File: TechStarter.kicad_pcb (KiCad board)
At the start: 2 copper layers, 57 parts, among them J10 Conn_01x03_Socket, J11 Conn_01x03_Socket, J3 Conn_01x02_Socket, J5 Conn_01x03_Socket, J7 Conn_01x03_Socket, J8 Conn_01x03_Socket, J9 Conn_01x03_Socket, Q3 IRLZ44N, U1 STM32F446RETx, U10 PC817, U2 TMC2209-LA, U3 TMC2209-LA, U4 LM2596S-3.3, U5 MX25L3233FM1, U6 TMC2209-LA, U7 AMS1117-3.3, U8 TMC2209-LA, U9 PC817

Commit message: .
.
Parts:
- removed BT1: Battery_Cell, Battery:BatteryHolder_ComfortableElectronic_CH273-2450_1x2450
- added C17: 680uF/35V, Capacitor_SMD:C_Elec_10x10.2, F.Cu at (150.1, 43.5)
- added C18: 220nF/6,3V, Capacitor_SMD:C_0603_1608Metric, F.Cu at (69.4, 102.5)
- added C19: 220nF/6,3V, Capacitor_SMD:C_0603_1608Metric, F.Cu at (69.4, 105.0)
- added C20: 220nF/6,3V, Capacitor_SMD:C_0603_1608Metric, F.Cu at (131.5, 126.5)
- added C21: 4,7uF, Capacitor_SMD:C_Elec_10x10.2, F.Cu at (200.5, 163.5)
- added C22: 220nF/6,3V, Capacitor_SMD:C_0603_1608Metric, F.Cu at (143.2, 75.5)
- added C23: 220nF/6,3V, Capacitor_SMD:C_0603_1608Metric, F.Cu at (143.2, 78.0)
- added J1: Conn_01x04_Socket, Connector_Phoenix_MC:PhoenixContact_MC_1,5_4-GF-3.81_1x04_P3.81mm_Horizontal_ThreadedFlange_MountHole, F.Cu at (261.0, 70.4)
- added J12: Conn_01x04_Pin, Connector_PinSocket_2.54mm:PinSocket_1x04_P2.54mm_Vertical_SMD_Pin1Left, F.Cu at (87.5, 122.0)
- added J13: Conn_01x02_Socket, Connector_Phoenix_MC:PhoenixContact_MC_1,5_2-GF-3.5_1x02_P3.50mm_Horizontal_ThreadedFlange_MountHole, F.Cu at (175.7, 29.4)
- added J14: Conn_01x04_Socket, Connector_JST:JST_XH_B4B-XH-A_1x04_P2.50mm_Vertical, F.Cu at (237.0, 127.8)
- added J15: Conn_01x04_Socket, Connector_JST:JST_XH_S4B-XH-A_1x04_P2.50mm_Horizontal, F.Cu at (230.2, 134.8)
- added J16: Conn_01x02_Socket, Connector_Phoenix_MC:PhoenixContact_MC_1,5_2-G-3.81_1x02_P3.81mm_Horizontal, F.Cu at (190.3, 29.4)
- added J17: Conn_01x02_Socket, Connector_JST:JST_XH_B2B-XH-A_1x02_P2.50mm_Vertical, F.Cu at (172.5, 124.2)
- added J18: Conn_01x04_Socket, Connector_JST:JST_XH_S4B-XH-A_1x04_P2.50mm_Horizontal, F.Cu at (243.8, 134.8)
- added J2: Conn_01x04_Socket, Connector_Phoenix_MC:PhoenixContact_MC_1,5_4-GF-3.81_1x04_P3.81mm_Horizontal_ThreadedFlange_MountHole, F.Cu at (261.1, 43.7)
- added J4: Conn_01x04_Socket, Connector_Phoenix_MC:PhoenixContact_MC_1,5_4-GF-3.81_1x04_P3.81mm_Horizontal_ThreadedFlange_MountHole, F.Cu at (261.0, 97.4)
- added J6: Conn_01x04_Socket, Connector_Phoenix_MC:PhoenixContact_MC_1,5_4-GF-3.81_1x04_P3.81mm_Horizontal_ThreadedFlange_MountHole, F.Cu at (261.1, 124.2)
- added L1: 33uH, Inductor_SMD:L_7.3x7.3_H4.5, F.Cu at (136.4, 78.6)
- added R13: 10k, Resistor_SMD:R_0603_1608Metric, F.Cu at (143.2, 80.5)
- added R13: 10, Resistor_SMD:R_0603_1608Metric, F.Cu at (69.4, 107.5)
- added R24: 10k, Resistor_SMD:R_0603_1608Metric, F.Cu at (69.4, 110.1)
- added R25: 10k, Resistor_SMD:R_0603_1608Metric, F.Cu at (69.4, 112.6)
- added R26: 20k, Resistor_SMD:R_0603_1608Metric, F.Cu at (143.2, 83.0)
- added R27: 10k, Resistor_SMD:R_0603_1608Metric, F.Cu at (143.2, 85.5)
- added R5: 10k, Resistor_SMD:R_0603_1608Metric, F.Cu at (144.7, 50.7)
- added R6: 10k, Resistor_SMD:R_0603_1608Metric, F.Cu at (144.7, 53.2)
- added TH1: Thermistor_NTC, Resistor_THT:R_Axial_DIN0204_L3.6mm_D1.6mm_P2.54mm_Vertical, F.Cu at (133.3, 84.6)
- added U11: AMS1117-3.3, Package_TO_SOT_SMD:SOT-223-3_TabPin2, F.Cu at (171.2, 75.8)
- added U12: TP4056-42-ESOP8, Package_SO:SOIC-8-1EP_3.9x4.9mm_P1.27mm_EP2.41x3.3mm_ThermalVias, F.Cu at (85.5, 104.6)
- added U13: AMS1117-3.3, Package_TO_SOT_SMD:SOT-223-3_TabPin2, F.Cu at (116.2, 89.0)
- J3: footprint Connector:JWT_A3963_1x02_P3.96mm_Vertical -> Connector_JST:JST_XH_S2B-XH-A_1x02_P2.50mm_Horizontal
- moved J3 192.7 mm to (254.5, 30.7), turned to 180 degrees
- moved J5 190.9 mm to (246.0, 30.7), turned to 180 degrees
- moved J9 186.3 mm to (257.2, 134.8)
- moved J7 168.1 mm to (235.0, 30.7), turned to 180 degrees
- moved J8 145.2 mm to (223.8, 30.7), turned to 180 degrees
- moved J10 110.6 mm to (212.8, 30.7), turned to 180 degrees
- moved J11 82.1 mm to (201.8, 30.7), turned to 180 degrees
- moved R2 37.6 mm to (219.4, 98.5)
- moved R11 37.6 mm to (202.5, 102.0)
- moved R12 37.6 mm to (202.5, 98.5)
- moved U1 37.6 mm to (211.5, 100.0)
- moved U5 37.6 mm to (211.0, 87.0)
- moved R20 30.7 mm to (189.5, 80.5)
- moved R21 30.7 mm to (196.5, 88.5)
- moved U10 30.7 mm to (200.3, 93.8)
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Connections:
- U1 pad 11: unconnected-(U1-PC3-Pad11) -> Vbat
- U1 pad 30: unconnected-(U1-VCAP_1-Pad30) -> Net-(U1-VCAP_1)
- U1 pad 60: unconnected-(U1-BOOT0-Pad60) -> Net-(U1-BOOT0)
- U1 pad 7: unconnected-(U1-NRST-Pad7) -> Net-(U1-NRST)
- U3 pad 1: Net-(J1-Pin_3) -> Net-(J1-Pin_4)
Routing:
- net +5V: track 0.00 -> 92.6 mm, vias 0 -> 6
- net motorEN: track 0.00 -> 75.8 mm, vias 0 -> 5
- net Net-(U4-FB): track 0.00 -> 74.9 mm
- net GND: track 128.6 -> 195.6 mm
- net Net-(J2-Pin_4): track 0.00 -> 54.4 mm, vias 0 -> 1
- net motor4dir: track 0.00 -> 52.2 mm, vias 0 -> 2
- net Net-(J2-Pin_3): track 0.00 -> 49.9 mm, vias 0 -> 1
- net motor3dir: track 0.00 -> 49.5 mm, vias 0 -> 2
- net +24V: track 95.0 -> 137.8 mm
- net Net-(J2-Pin_2): track 0.00 -> 41.9 mm, vias 0 -> 1
- net RX1/TX1: track 2.73 -> 42.7 mm, vias 0 -> 4
- net Net-(J2-Pin_1): track 0.00 -> 39.9 mm, vias 0 -> 1
- net Net-(J1-Pin_4): track 0.00 -> 39.5 mm
- net Net-(J4-Pin_4): track 0.00 -> 27.1 mm, vias 0 -> 1
- net Net-(J6-Pin_4): track 0.00 -> 25.5 mm, vias 0 -> 1
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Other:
- board outline added: 100 x 112.8 mm
- copper layers 2 -> 4

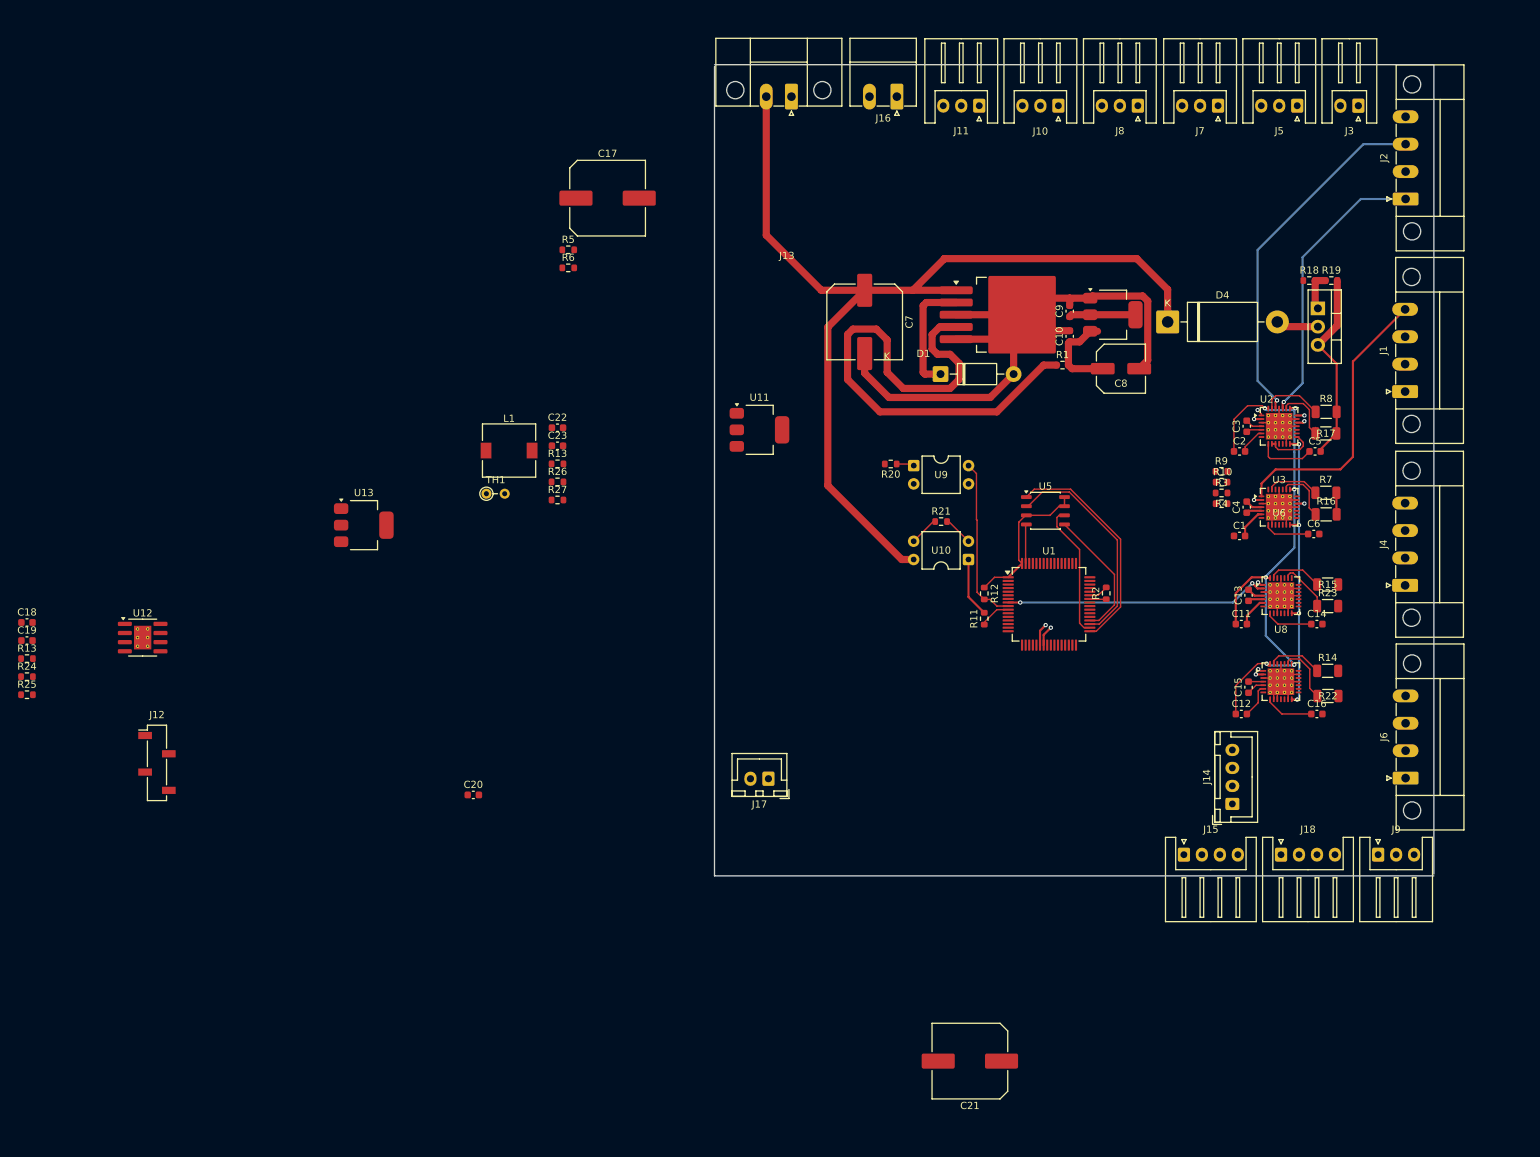
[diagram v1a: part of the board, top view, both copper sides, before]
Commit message: RIP
reason of death
too much of board for too little time...
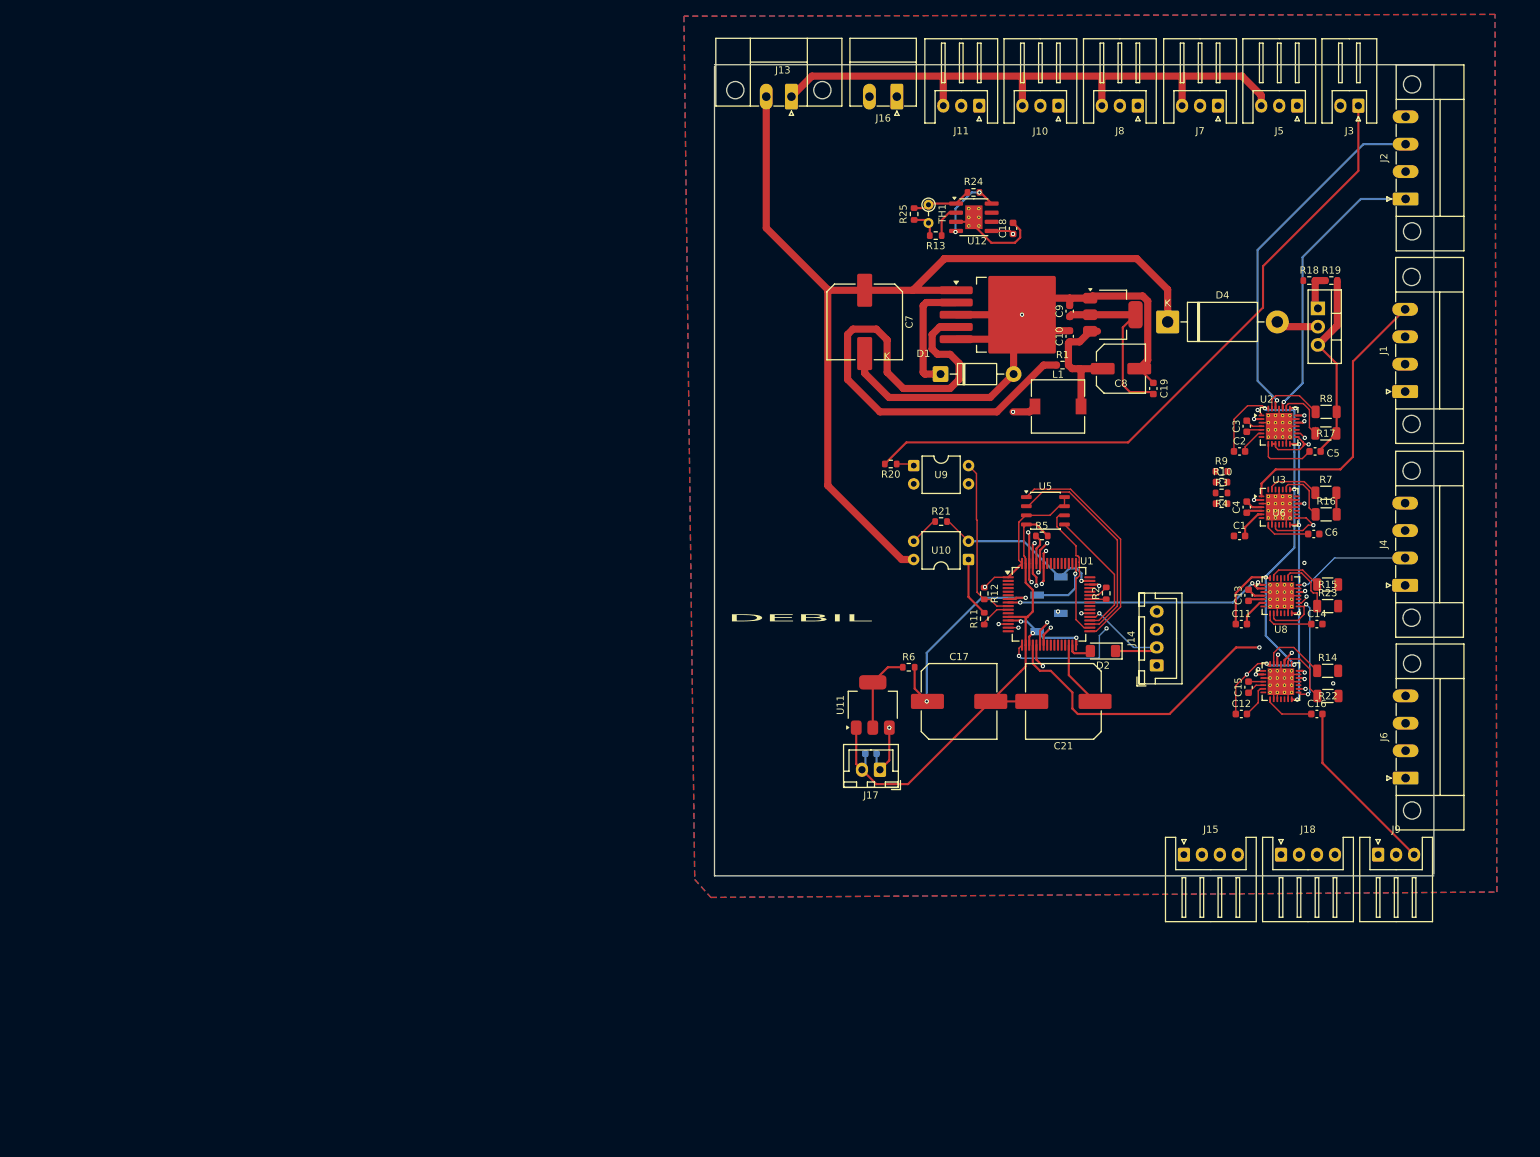
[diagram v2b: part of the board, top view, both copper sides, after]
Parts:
- removed C22, C23: 220nF/6,3V, Capacitor_SMD:C_0603_1608Metric
- removed the R13 at (143.2, 80.5)
- removed the R13 at (69.4, 107.5)
- removed R26: 20k, Resistor_SMD:R_0603_1608Metric
- removed R27: 10k, Resistor_SMD:R_0603_1608Metric
- removed U13: AMS1117-3.3, Package_TO_SOT_SMD:SOT-223-3_TabPin2
- added D2: D_Zener, Diode_SMD:D_MiniMELF, F.Cu at (219.0, 106.5)
- added R13: 10k, Resistor_SMD:R_0603_1608Metric, F.Cu at (195.8, 48.8)
- C20, J12: moved to B.Cu
- moved C19 160.4 mm to (226.0, 70.0), turned to 90 degrees
- moved R24 147.8 mm to (201.0, 42.8), turned to 180 degrees
- moved C18 147.6 mm to (206.5, 47.8), turned to 90 degrees
- moved R25 140.3 mm to (192.8, 45.8), turned to -90 degrees
- moved U12 129.5 mm to (201.1, 46.2)
- moved J12 125.9 mm to (211.5, 100.0)
- moved C17 85.3 mm to (199.0, 113.5)
- moved R5 76.9 mm to (210.5, 90.5)
- moved L1 76.6 mm to (212.8, 72.5)
- moved TH1 73.4 mm to (194.8, 44.5), turned to -90 degrees
- moved R6 73.0 mm to (192.0, 108.8)
- moved C20 55.6 mm to (186.8, 120.8), turned to 180 degrees
- moved C21 51.7 mm to (213.5, 113.5)
- moved U11 41.4 mm to (187.0, 114.0), turned to 90 degrees
- moved J14 21.9 mm to (226.5, 108.5)
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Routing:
- net GND: track 195.6 -> 588.3 mm, vias 0 -> 2
- net +3.3V: track 36.7 -> 231.0 mm, vias 0 -> 9
- net Net-(J3-Pin_2): track 4.12 -> 100.8 mm
- net Net-(J3-Pin_1): track 0.00 -> 95.1 mm
- net +BATT: track 0.00 -> 88.4 mm, vias 0 -> 2
- net Net-(D4-A): track 5.91 -> 75.6 mm
- net EB2: track 0.00 -> 68.6 mm, vias 0 -> 2
- net EB4: track 0.00 -> 64.5 mm, vias 0 -> 2
- net EB1: track 0.00 -> 63.1 mm, vias 0 -> 2
- net motor4step: track 0.00 -> 61.6 mm, vias 0 -> 3
- net EB3: track 0.00 -> 53.2 mm, vias 0 -> 2
- net motor1dir: track 0.00 -> 52.8 mm, vias 0 -> 2
- net motor1step: track 0.00 -> 50.6 mm, vias 0 -> 2
- net motor2dir: track 0.00 -> 50.0 mm, vias 0 -> 2
- net motor2step: track 0.00 -> 46.7 mm, vias 0 -> 2
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- added copper zone on B.Cu, net GND
- added copper zone on F.Cu, net GND
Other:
- board text added: "DEBIL"

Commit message: board - done
still gotta remove the errrors
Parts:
- moved R9 15.3 mm to (222.1, 89.1)
- moved R3 13.4 mm to (222.2, 85.6)
- moved R10 12.8 mm to (223.4, 87.3)
- moved R4 12.3 mm to (223.3, 83.9)
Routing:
- net +3.3V: track 231.0 -> 427.4 mm, vias 9 -> 16
- net +5V: track 121.0 -> 215.2 mm, vias 9 -> 14
- net IS3: track 0.00 -> 82.2 mm, vias 0 -> 2
- net IS4: track 0.00 -> 82.0 mm, vias 0 -> 2
- net IS2: track 0.00 -> 76.0 mm, vias 0 -> 2
- net IS5: track 0.00 -> 73.0 mm, vias 0 -> 1
- net IS6: track 0.00 -> 69.5 mm, vias 0 -> 1
- net Inductor: track 0.00 -> 63.2 mm, vias 0 -> 2
- net IS1: track 0.00 -> 61.0 mm, vias 0 -> 1
- net motor3step: track 0.00 -> 53.2 mm, vias 0 -> 4
- net Net-(J4-Pin_1): track 0.00 -> 32.0 mm, vias 0 -> 1
- net Net-(J1-Pin_3): track 0.00 -> 31.0 mm, vias 0 -> 1
- net RX1/TX1: track 42.7 -> 71.2 mm, vias 4 -> 8
- net Net-(J1-Pin_2): track 0.00 -> 25.2 mm, vias 0 -> 1
- net Net-(J1-Pin_1): track 0.00 -> 23.4 mm, vias 0 -> 2
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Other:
- board text removed: "DEBIL"

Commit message: .
GANG BANG
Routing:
- net GND: track 595.1 -> 596.0 mm, vias 2 -> 838
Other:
- board size 100 x 112.8 mm -> 100 x 112.5 mm

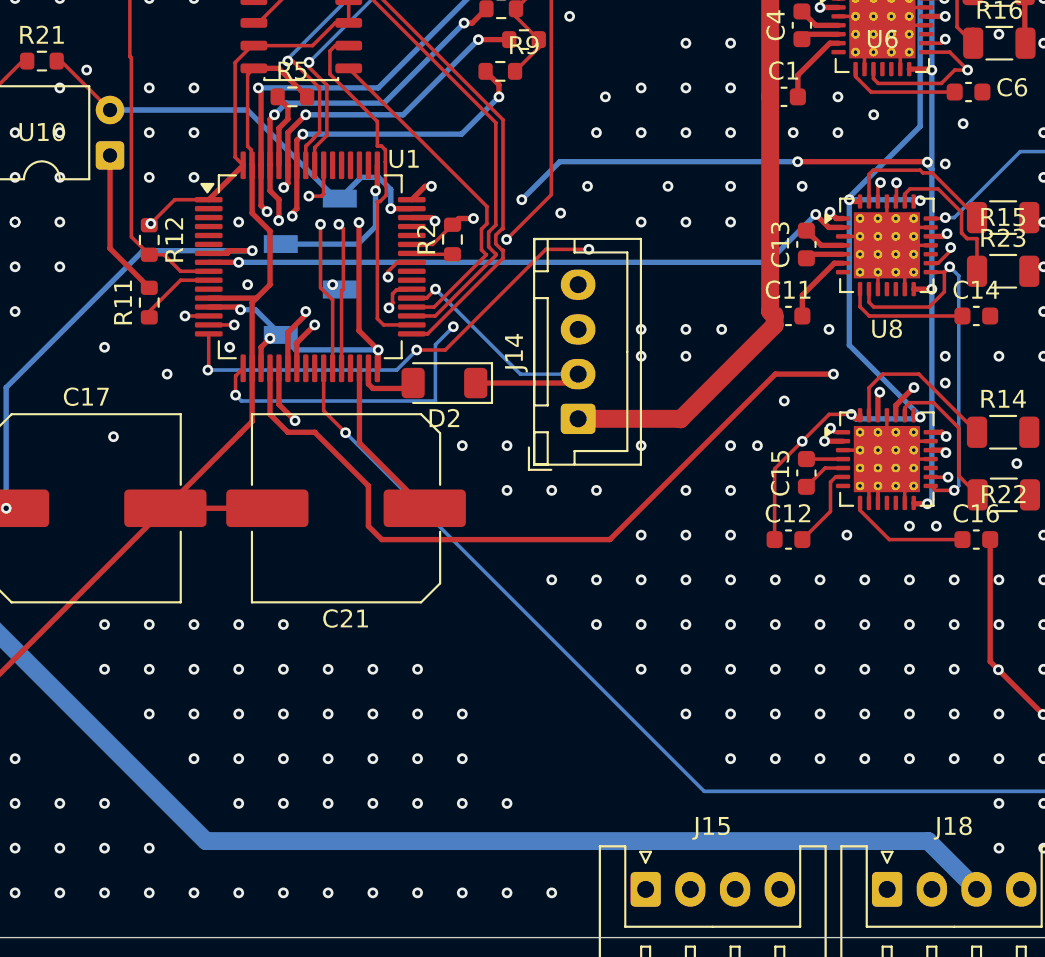
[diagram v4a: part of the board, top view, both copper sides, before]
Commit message: Programovací konektor
Hodil jsem ho normálně ...
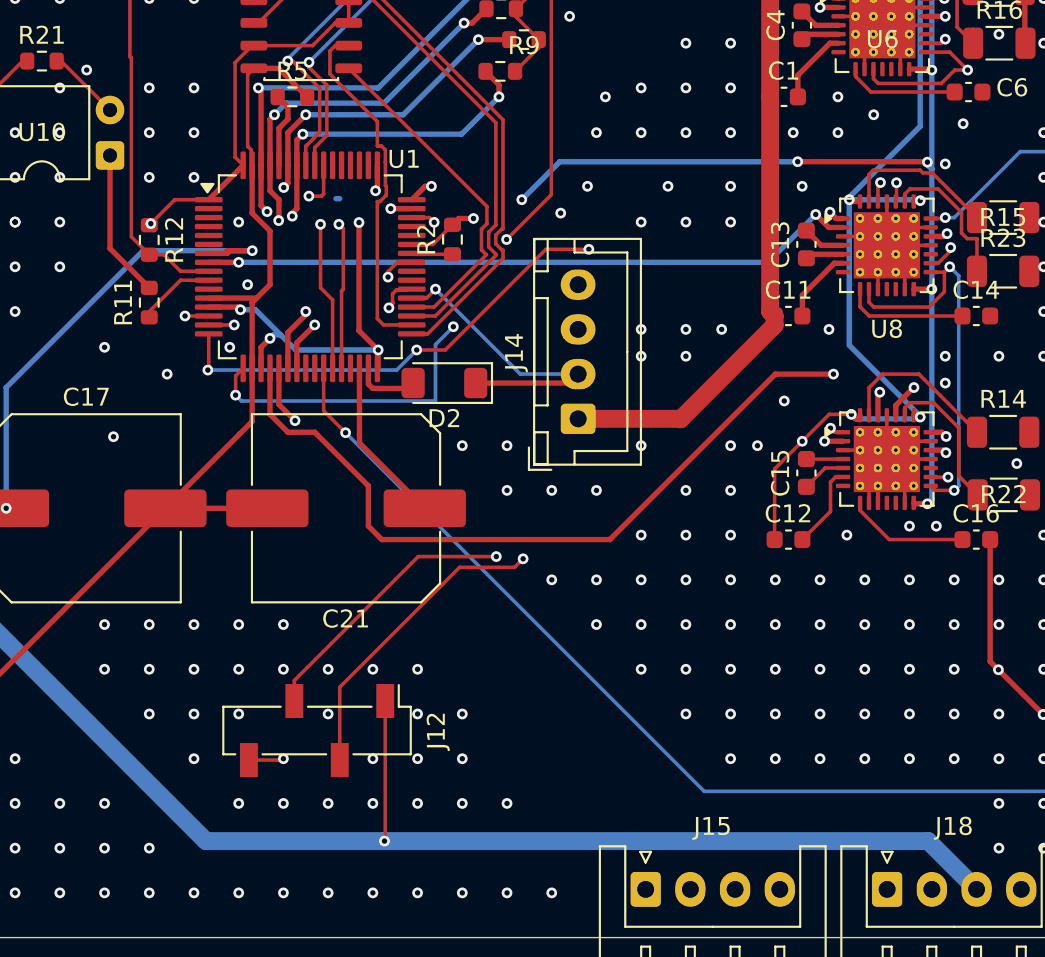
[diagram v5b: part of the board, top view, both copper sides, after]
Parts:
- J12: moved to F.Cu
- moved J12 25.9 mm to (211.9, 125.9), turned to -90 degrees
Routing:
- net SWDIO: track 9.09 -> 46.9 mm
- net SWCLK: track 9.17 -> 40.0 mm, vias 1 -> 2
- net GND: track 596.0 -> 578.6 mm, vias 838 -> 834
- net +3.3V: track 427.4 -> 435.3 mm, vias 16 -> 17

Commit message: Capacitor + other stuff
Did a safe of your ass
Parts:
- C17: value 680uF/35V -> 100n/6,3V; footprint Capacitor_SMD:C_Elec_10x10.2 -> Capacitor_SMD:C_0603_1608Metric
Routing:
- net Net-(U1-NRST): track 31.9 -> 35.6 mm
- net GND: track 578.6 -> 581.2 mm, vias 834 -> 849
